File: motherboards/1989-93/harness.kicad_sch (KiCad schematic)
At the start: 7 parts, among them J1 TE 174917-6

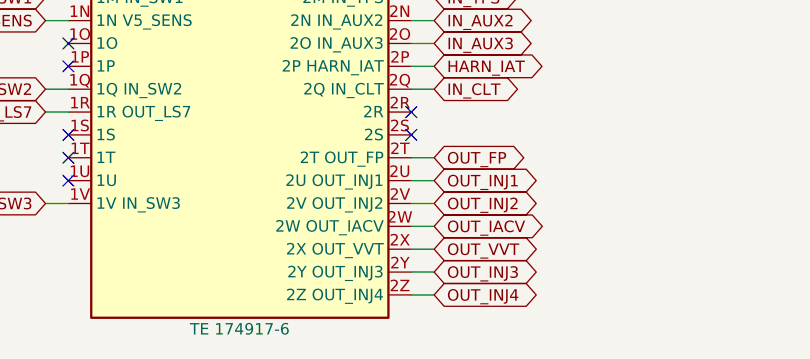
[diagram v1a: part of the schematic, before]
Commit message: Rev 0.5 daughterboard, rev 0.6 1989-93/1994-95 motherboards: review fixes
Daughterboard rev 0.5:
- SN74LVC4245A drives the eight AUIPS2041 low sides at 5 V; output enable pulled
  off (R71) until the firmware enables it on PA8.
- BOOT1 pull-down (R72); hall input clamps D13/D14.
- ULN2003 COM to an SMAJ33A TVS (D11) instead of +12V: no key-off back-feed,
  no conduction in a 35 V load dump.
- Logic supply: D7/D8 -> 0.5 A PTC F1 -> SMAJ33A D12; C16 50 V, SS36 D9, C59.
- Tach stays an output.

Motherboards:
- Idle/VVT freewheel diodes, 4.7k switch pull-up options (not fitted),
  AUX VBAT PTC on all years.
- 1989-93 rev 0.6: two drivers per injector wire (0R links), SMCJ40A clamps.
- 2001-05: J1 3B tied to 3A.

Firmware: low-side enable (inverted open drain, forced writes, off during
configuration changes), unused control pins parked with pull-down, 1989-93
batch on all four outputs, VBATT offset noted.

Verification: 18/18 board tests, 119/119 harness check, circuit sims
20 OK / 3 CHECK / 6 REF / 0 FAIL, flash sim 9/9, firmware and bootloader
build; all boards 0 unconnected, 0 clearance errors.

Co-Authored-By: Claude Opus 5.5 <noreply@anthropic.com>
Claude-Session: https://claude.ai/code/session_012UFcA8PhPqkqYxcgEjD2n9
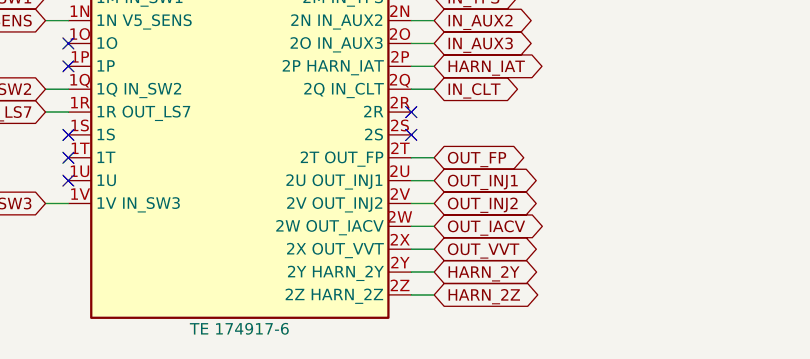
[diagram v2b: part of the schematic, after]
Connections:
- net OUT_INJ3 renamed HARN_2Y
- net OUT_INJ4 renamed HARN_2Z
